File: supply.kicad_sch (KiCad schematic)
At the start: 165 parts, among them J10001 JST_SH_1x4_BM04B-SRSS-TB-LF-SN, J1001 BarrelJack_3167288, Q10001 BSS138PW, Q10002 SI7613DN-T1-GE3, Q10003 BSS138PW, Q1001 SI7613DN-T1-GE3, Q1002 BSS138PW, Q20001 BSS138PW, SW10001 SW_DPDT_JS202011JCQN_SMD, SW10002 CVS-03B, SW1001 SW_CVS-02B, SW1002 SW_KMR211NGLFS_SMD, U10001 NCP718BSN330T1G, U10002 MPM54304GMN, U10003 MPM54304GMN, U10004 MAX16150A_SOT, U10005 LTC4412IS6, U10006 LM3880, U10007 MP8869S, U10008 XC6230H001ER-G, U10009 MAX812REUS+T, U1001 LTC4412IS6, U10010 PAC1954T-E_VQFN, U10011 PAC1954T-E_VQFN, U10012 MCP4726A0T-E_MAY

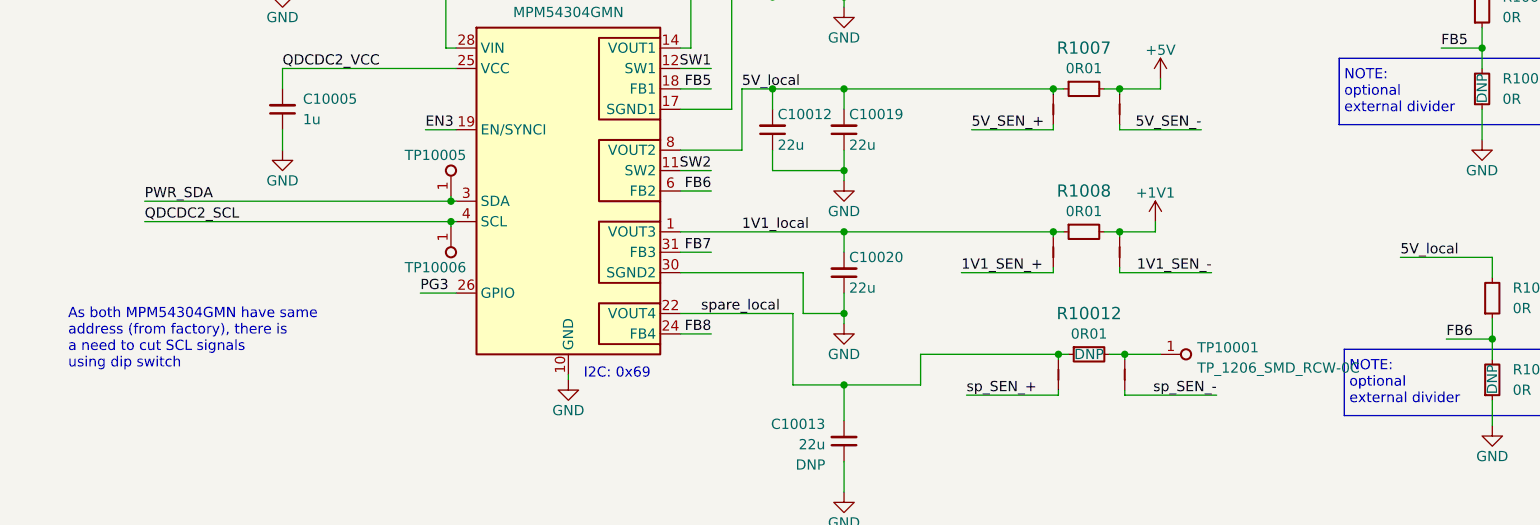
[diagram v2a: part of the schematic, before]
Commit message: Finish routing after schematic modification, optimize power planes
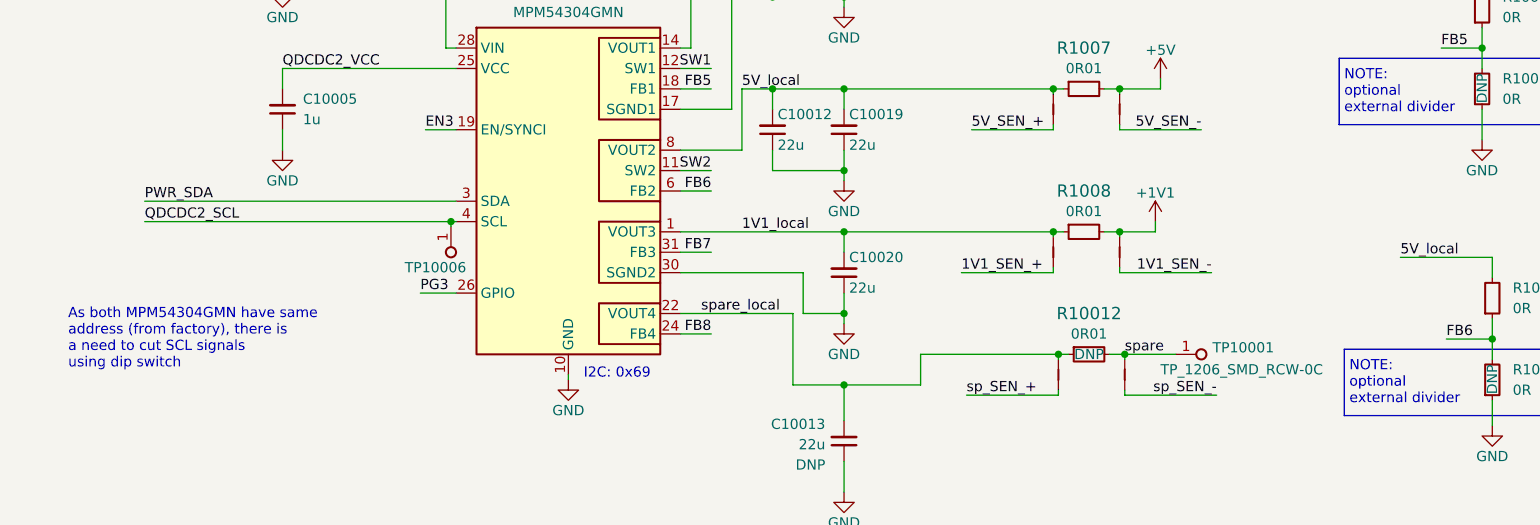
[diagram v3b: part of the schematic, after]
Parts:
- removed TP10005: TP_0.75mm_SMD, sodimm-ddr5-tester-footprints:TP_SMD_0.75mm, symbol sodimm-ddr5-tester:TP_0.75mm_SMD
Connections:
- net spare: now reaches NT10002.2, R10012.2, TP10001.1
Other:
- moved on the sheet: TP10001
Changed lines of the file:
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@@
   (junction (at 350.52 311.785) (diameter 0) (color 0 0 0 0)
   )
-  (junction (at 73.025 215.9) (diameter 0) (color 0 0 0 0)
-  )
   (junction (at 113.03 180.34) (diameter 0) (color 0 0 0 0)
   )
@@
     (stroke (width 0) (type default) (color 0 0 0 0))
   )
-  (wire (pts (xy 156.845 234.95) (xy 161.29 234.95))
+  (wire (pts (xy 156.845 234.95) (xy 163.195 234.95))
     (stroke (width 0) (type default) (color 0 0 0 0))
   )
@@
     (stroke (width 0) (type default) (color 0 0 0 0))
   )
-  (wire (pts (xy 73.025 215.9) (xy 73.025 215.265))
-    (stroke (width 0) (type default) (color 0 0 0 0))
-  )
   (wire (pts (xy 116.84 224.79) (xy 116.84 229.87))
     (stroke (width 0) (type default) (color 0 0 0 0))
@@
     (stroke (width 0) (type default) (color 0 0 0 0))
   )
-  (wire (pts (xy 73.025 215.9) (xy 73.66 215.9))
-    (stroke (width 0) (type default) (color 0 0 0 0))
-  )
   (wire (pts (xy 155.575 56.515) (xy 155.575 55.245))
     (stroke (width 0) (type default) (color 0 0 0 0))
@@
     (stroke (width 0) (type default) (color 0 0 0 0))
   )
-  (wire (pts (xy 34.925 215.9) (xy 73.025 215.9))
+  (wire (pts (xy 34.925 215.9) (xy 73.66 215.9))
     (stroke (width 0) (type default) (color 0 0 0 0))
   )
@@
     (effects (font (size 1.27 1.27)) (justify right bottom))
   )
+  (label "spare" (at 156.845 234.95 0)
+    (effects (font (size 1.27 1.27)) (justify left bottom))
+  )
   (label "PWR_SCL" (at 278.765 221.615 0)
     (effects (font (size 1.27 1.27)) (justify left bottom))
@@
     (pin "1")
   )
-  (symbol (lib_id "sodimm-ddr5-tester:TP_0.75mm_SMD") (at 73.025 215.265 90) (unit 1)
-    (in_bom yes) (on_board yes)
-    (property "Reference" "TP10005" (id 0) (at 74.93 210.185 90)
-      (effects (font (size 1.27 1.27)) (justify left))
-    )
-    (property "Value" "TP_0.75mm_SMD" (id 1) (at 75.565 215.265 0)
-      (effects (font (size 1.27 1.27)) hide)
-    )
-    (property "Footprint" "sodimm-ddr5-tester-footprints:TP_SMD_0.75mm" (id 2) (at 67.945 210.185 0)
-      (effects (font (size 1.27 1.27)) (justify left) hide)
-    )
-    (property "Datasheet" "" (id 3) (at 65.405 210.185 0)
-      (effects (font (size 1.27 1.27)) (justify left) hide)
-    )
-    (property "MPN" "" (id 4) (at 73.025 215.265 0)
-      (effects (font (size 1.27 1.27)) hide)
-    )
-    (property "Manufacturer" "" (id 5) (at 73.025 215.265 0)
-      (effects (font (size 1.27 1.27)) hide)
-    )
-    (property "Author" "Antmicro" (id 6) (at 88.265 200.025 0)
-      (effects (font (size 1.27 1.27) (thickness 0.15)) (justify left bottom) hide)
-    )
-    (property "License" "Apache-2.0" (id 7) (at 90.805 200.025 0)
-      (effects (font (size 1.27 1.27) (thickness 0.15)) (justify left bottom) hide)
-    )
-    (pin "1")
-  )
   (symbol (lib_id "sodimm-ddr5-tester:VDC") (at 52.07 178.435 0) (unit 1)
     (in_bom yes) (on_board yes) (fields_autoplaced)
@@
     (pin "1")
   )
-  (symbol (lib_id "antmicroTestPoints:TP_1206_SMD_RCW-0C") (at 161.29 234.95 0) (unit 1)
-    (in_bom yes) (on_board yes) (fields_autoplaced)
-    (property "Reference" "TP10001" (id 0) (at 165.862 234.1194 0)
+  (symbol (lib_id "antmicroTestPoints:TP_1206_SMD_RCW-0C") (at 163.195 234.95 0) (unit 1)
+    (in_bom yes) (on_board yes)
+    (property "Reference" "TP10001" (id 0) (at 167.767 234.1194 0)
       (effects (font (size 1.27 1.27) (thickness 0.15)) (justify left))
     )
-    (property "Value" "TP_1206_SMD_RCW-0C" (id 1) (at 165.862 236.6431 0)
+    (property "Value" "TP_1206_SMD_RCW-0C" (id 1) (at 161.29 236.855 0)
       (effects (font (size 1.27 1.27) (thickness 0.15)) (justify left))
     )
-    (property "Footprint" "antmicro-footprints:TP_1206_SMD_RCW-0C" (id 2) (at 179.07 245.11 0)
+    (property "Footprint" "antmicro-footprints:TP_1206_SMD_RCW-0C" (id 2) (at 180.975 245.11 0)
       (effects (font (size 1.27 1.27) (thickness 0.15)) (justify left bottom) hide)
     )
-    (property "Datasheet" "https://www.te.com/commerce/DocumentDelivery/DDEController?Action=srchrtrv&DocNm=1773266&DocType=DS&DocLang=English" (id 3) (at 179.07 247.65 0)
+    (property "Datasheet" "https://www.te.com/commerce/DocumentDelivery/DDEController?Action=srchrtrv&DocNm=1773266&DocType=DS&DocLang=English" (id 3) (at 180.975 247.65 0)
       (effects (font (size 1.27 1.27) (thickness 0.15)) (justify left bottom) hide)
     )
-    (property "MPN" "RCW-0C" (id 4) (at 179.07 250.19 0)
+    (property "MPN" "RCW-0C" (id 4) (at 180.975 250.19 0)
       (effects (font (size 1.27 1.27) (thickness 0.15)) (justify left bottom) hide)
     )
-    (property "Manufacturer" "TE Connectivity" (id 5) (at 179.07 252.73 0)
+    (property "Manufacturer" "TE Connectivity" (id 5) (at 180.975 252.73 0)
       (effects (font (size 1.27 1.27) (thickness 0.15)) (justify left bottom) hide)
     )
-    (property "Author" "Antmicro" (id 6) (at 179.07 255.27 0)
+    (property "Author" "Antmicro" (id 6) (at 180.975 255.27 0)
       (effects (font (size 1.27 1.27) (thickness 0.15)) (justify left bottom) hide)
     )
-    (property "License" "Apache-2.0" (id 7) (at 179.07 257.81 0)
+    (property "License" "Apache-2.0" (id 7) (at 180.975 257.81 0)
       (effects (font (size 1.27 1.27) (thickness 0.15)) (justify left bottom) hide)
     )

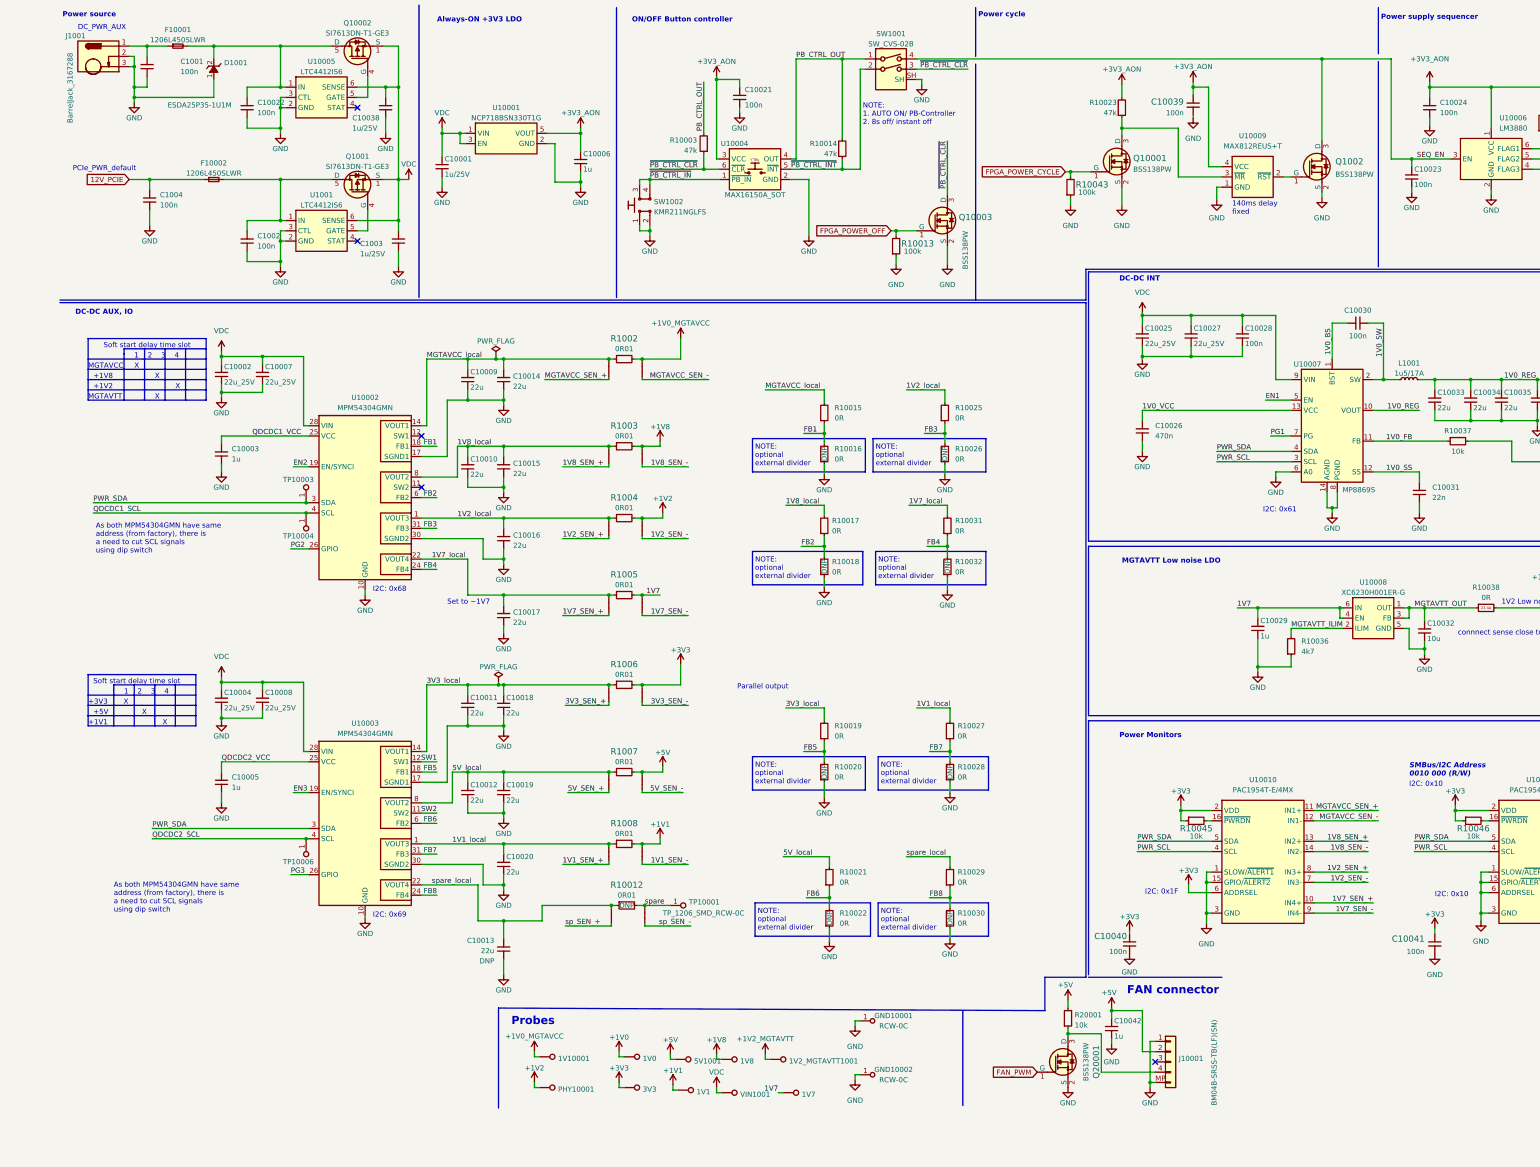
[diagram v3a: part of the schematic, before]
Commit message: Optimize BOM, replace obsolete parts, improve manufacturing attributes
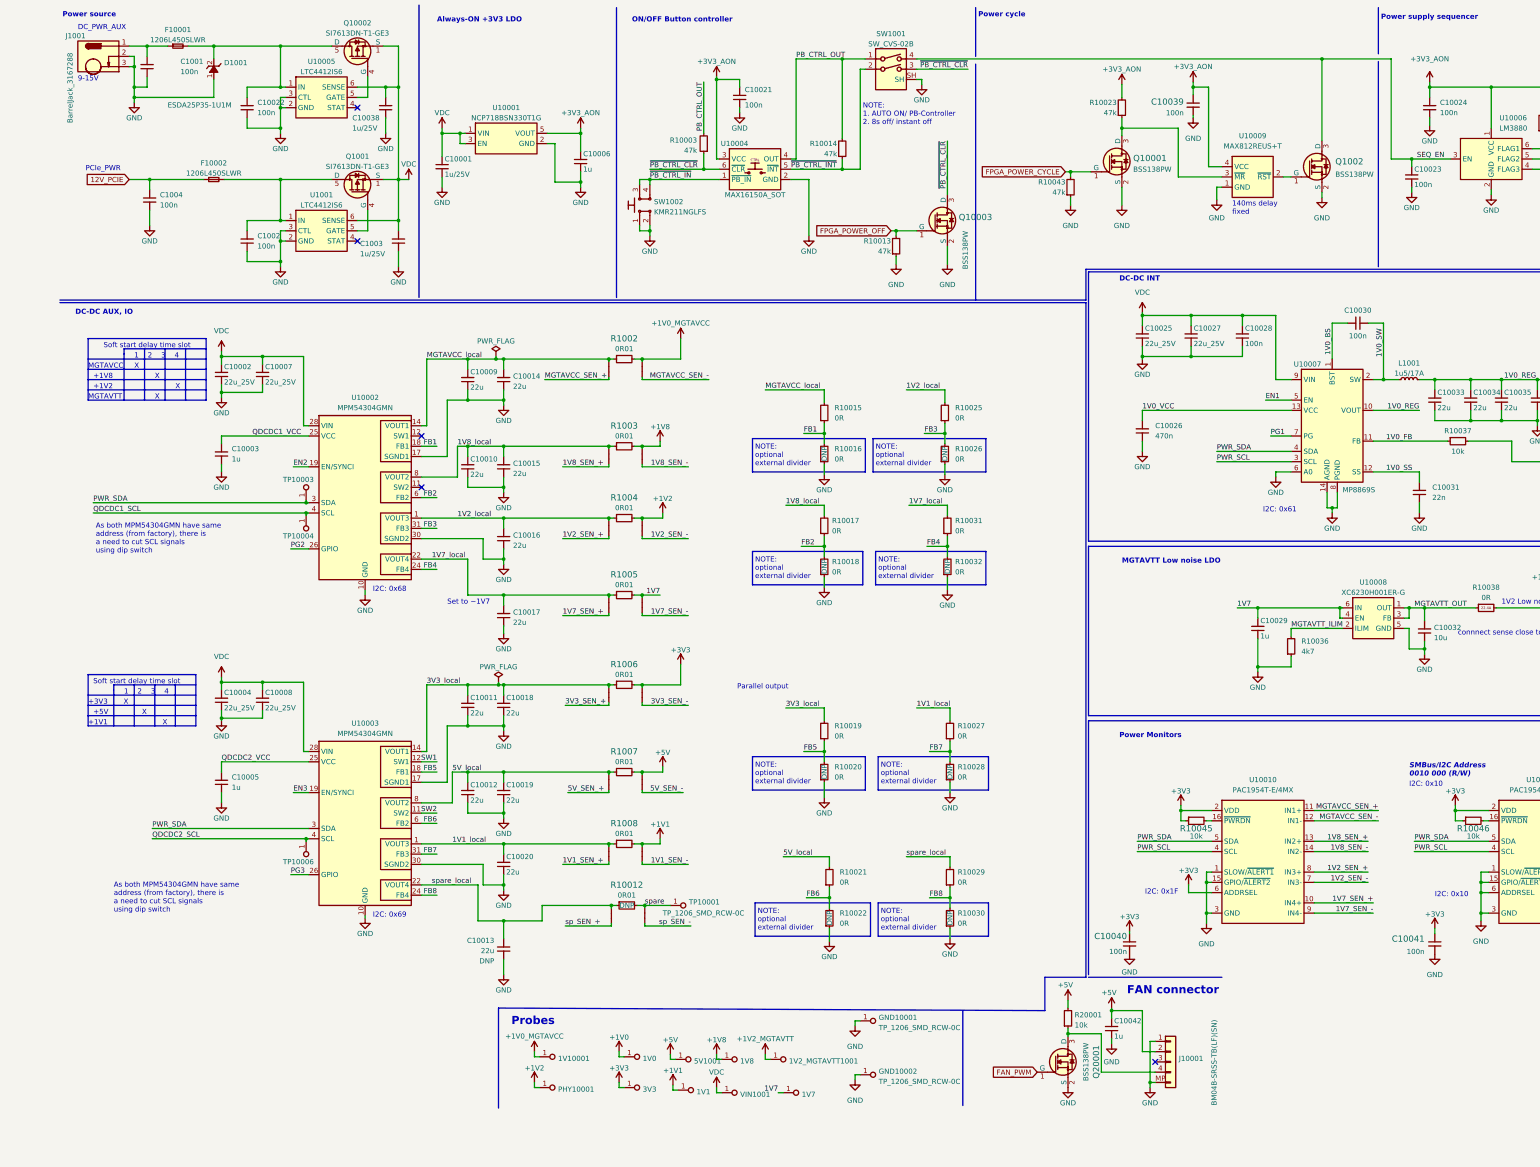
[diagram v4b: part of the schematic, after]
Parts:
- removed C10032: C_10u_0402, sodimm-ddr5-tester-footprints:C_0402_1005Metric, symbol sodimm-ddr5-tester:C_10u_0402
- removed GND10001, GND10002: TestPoint_Probe_1206_RCW-0C, sodimm-ddr5-tester-footprints:PROBE_PAD_1206, symbol sodimm-ddr5-tester:TestPoint_Probe_1206_RCW-0C
- removed R10013, R10043: R_100k_0402, sodimm-ddr5-tester-footprints:R_0402_1005Metric, symbol sodimm-ddr5-tester:R_100k_0402
- added C10032: C_10u_6.3V_0402, antmicro-footprints:C_0402_1005Metric, symbol antmicroCapacitors0402:C_10u_6.3V_0402
- added GND10001, GND10002: TP_1206_SMD_RCW-0C, antmicro-footprints:TP_1206_SMD_RCW-0C, symbol antmicroTestPoints:TP_1206_SMD_RCW-0C
- added R10013, R10043: R_47k_0402, sodimm-ddr5-tester-footprints:R_0402_1005Metric, symbol sodimm-ddr5-tester:R_47k_0402
- 1V0, 1V1, 1V10001, 1V2_MGTAVTT1001, 1V7, 1V8, 3V3, 5V1001, PHY10001, VIN1001: footprint sodimm-ddr5-tester-footprints:Testpoint_smd_1mm -> antmicro-footprints:TP_SMD_1mm; symbol sodimm-ddr5-tester:TP_1mm_SMD -> antmicroTestPoints:TP_1mm_SMD
- TP10003, TP10004, TP10006: footprint sodimm-ddr5-tester-footprints:TP_SMD_0.75mm -> antmicro-footprints:TP_SMD_0.75mm; symbol sodimm-ddr5-tester:TP_0.75mm_SMD -> antmicroTestPoints:TP_0.75mm_SMD
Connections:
- net FPGA_POWER_CYCLE: now also R10043.2
- net FPGA_POWER_OFF: now also R10013.2
- net GND: now also C10032.1, GND10001.1, GND10002.1, R10013.1, R10043.1
- net MGTAVTT_OUT: now also C10032.2
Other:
- note added: "9-15V"
- note added: "PCIe_PWR"
- note removed: "PCIe_PWR_default"

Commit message: Fix ETH PHY sequencing
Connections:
- net +1V2: now also NT10002.2, R10012.2; no longer NT1010.2, R1004.2
- net 1V2_SEN_+: now also NT10001.1, U10011.10 (IN4+); no longer NT1003.1, U10010.8 (IN3+)
- net 1V2_SEN_-: now also NT10002.1, U10011.9 (IN4-); no longer NT1010.1, U10010.7 (IN3-)
- net 1V2_local: now also C10013.2, NT10001.2, R10012.1, R10029.2, U10003.22 (VOUT4), U10003.23 (VOUT4); no longer C10016.2, NT1003.2, R10025.2, R1004.1, U10002.1 (VOUT3), U10002.32 (VOUT3)
- net sp_SEN_+: now also NT1003.1, U10010.8 (IN3+); no longer NT10001.1, U10011.10 (IN4+)
- net sp_SEN_-: now also NT1010.1, U10010.7 (IN3-); no longer NT10002.1, U10011.9 (IN4-)
- net spare: now also NT1010.2, R1004.2; no longer NT10002.2, R10012.2
- net spare_local: now also C10016.2, NT1003.2, R10025.2, R1004.1, U10002.1 (VOUT3), U10002.32 (VOUT3); no longer C10013.2, NT10001.2, R10012.1, R10029.2, U10003.22 (VOUT4), U10003.23 (VOUT4)
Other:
- moved on the sheet: TP10001

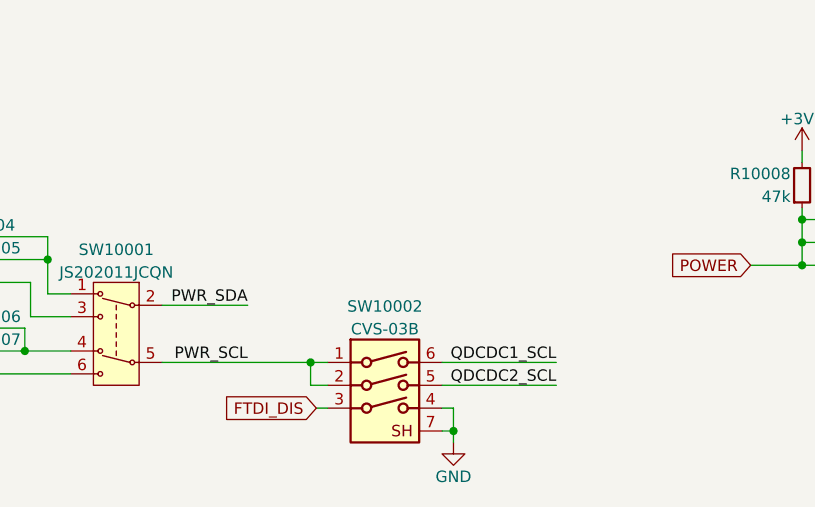
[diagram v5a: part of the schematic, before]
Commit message: Improve QSPI termination, improve power I2C WiP
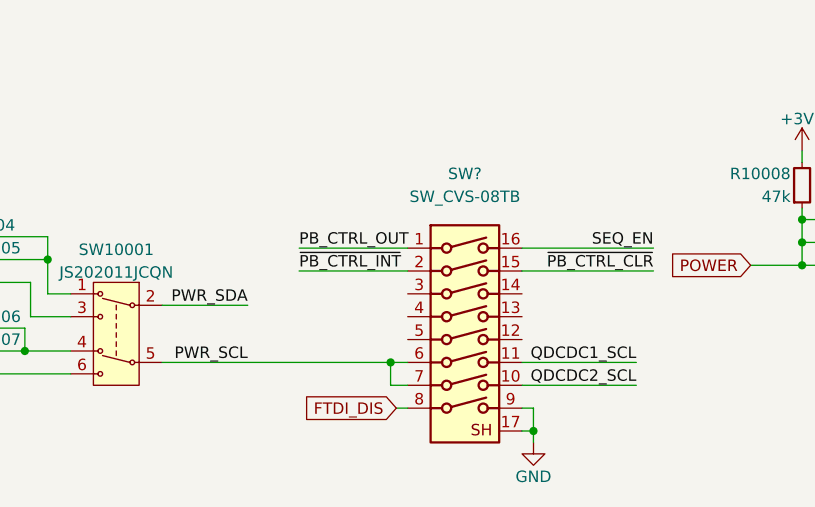
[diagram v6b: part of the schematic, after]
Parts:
- removed SW10002: CVS-03B, antmicro-footprints:SW_DIP_SPSTx03_Slide_Copal_CVS-03xB_W5.9mm_P1mm, symbol antmicroSlideSwitches:CVS-03B
- added SW?: SW_CVS-08TB, antmicro-footprints:SW_DIP_SPSTx08_Slide_Copal_CVS-08xB_W5.9mm_P1mm, symbol SlideSwitches:SW_CVS-08TB
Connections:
- net FTDI_DIS: now also SW?.8
- net GND: now also SW?.17, SW?.9
- net PB_CTRL_OUT: now also SW?.1
- net PWR_SCL: now also SW?.6, SW?.7
- net QDCDC1_SCL: now also SW?.11
- net QDCDC2_SCL: now also SW?.10
- net SEQ_EN: now also SW?.16
- net ~{PB_CTRL_CLR}: now also SW?.15
- net ~{PB_CTRL_INT}: now also SW?.2
